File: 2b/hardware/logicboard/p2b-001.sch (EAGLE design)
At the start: 76 parts, among them IC1 74LS06N, IC2 4066N, J1 MKR, J10 1-Wire, J2 GPIO, J20 GPIO, J3 Vcc, J4** RLY2, J5 SPI, J6 LED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

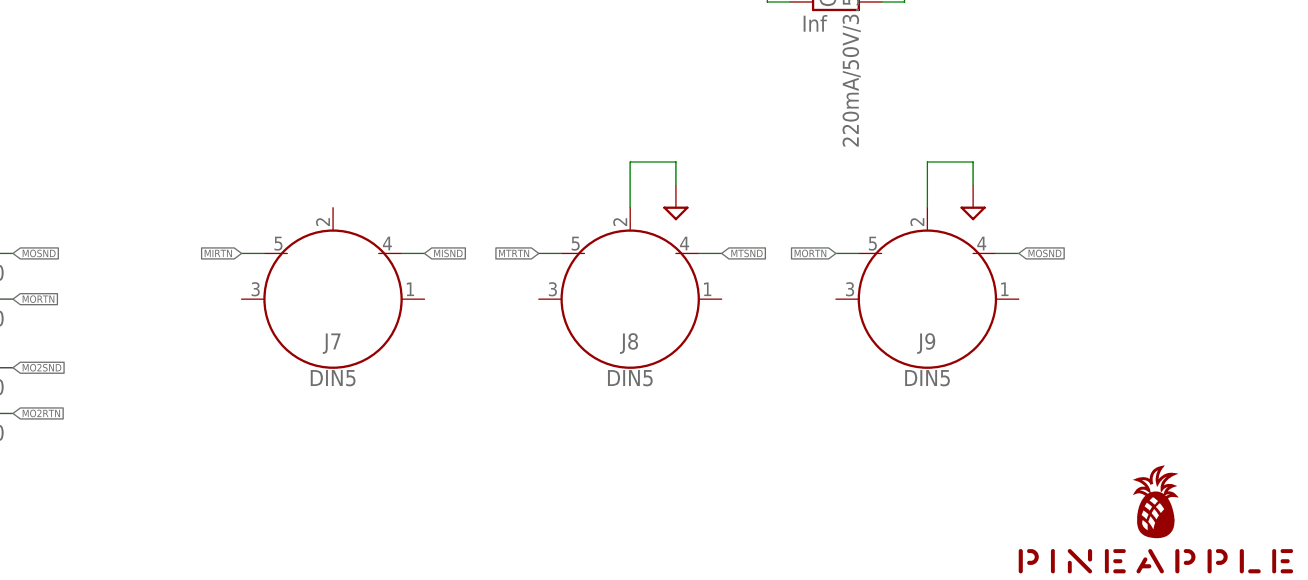
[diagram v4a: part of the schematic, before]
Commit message: Now P2b has phantom power.
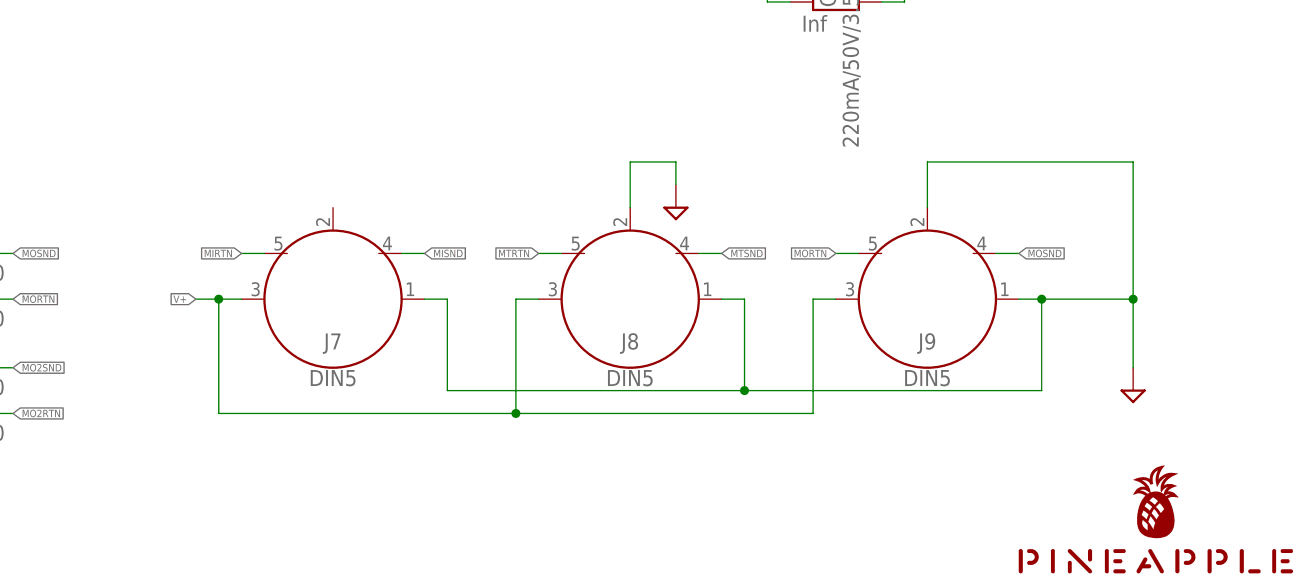
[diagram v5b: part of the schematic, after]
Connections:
- net GND: now also J7.1, J8.1, J9.1
- net V+: now also J7.3, J8.3, J9.3
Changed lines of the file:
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@@
 </instance>
 <instance part="SUPPLY16" gate="GND" x="259.08" y="48.26" smashed="yes"/>
-<instance part="SUPPLY17" gate="GND" x="292.1" y="48.26" smashed="yes"/>
+<instance part="SUPPLY17" gate="GND" x="309.88" y="27.94" smashed="yes"/>
 <instance part="SUPPLY19" gate="G$1" x="167.64" y="170.18" smashed="yes">
 <attribute name="VALUE" x="167.64" y="175.26" size="1.778" layer="96" align="bottom-center"/>
@@
 <pinref part="J9" gate="G$1" pin="2"/>
 <wire x1="287.02" y1="48.26" x2="287.02" y2="53.34" width="0.1524" layer="91"/>
-<wire x1="287.02" y1="53.34" x2="292.1" y2="53.34" width="0.1524" layer="91"/>
+<wire x1="287.02" y1="53.34" x2="309.88" y2="53.34" width="0.1524" layer="91"/>
 <pinref part="SUPPLY17" gate="GND" pin="GND"/>
-<wire x1="292.1" y1="53.34" x2="292.1" y2="50.8" width="0.1524" layer="91"/>
+<wire x1="309.88" y1="53.34" x2="309.88" y2="38.1" width="0.1524" layer="91"/>
+<pinref part="J9" gate="G$1" pin="1"/>
+<wire x1="309.88" y1="38.1" x2="309.88" y2="30.48" width="0.1524" layer="91"/>
+<wire x1="297.18" y1="38.1" x2="299.72" y2="38.1" width="0.1524" layer="91"/>
+<junction x="309.88" y="38.1"/>
+<pinref part="J8" gate="G$1" pin="1"/>
+<wire x1="299.72" y1="38.1" x2="309.88" y2="38.1" width="0.1524" layer="91"/>
+<wire x1="264.16" y1="38.1" x2="266.7" y2="38.1" width="0.1524" layer="91"/>
+<wire x1="266.7" y1="38.1" x2="266.7" y2="27.94" width="0.1524" layer="91"/>
+<wire x1="266.7" y1="27.94" x2="299.72" y2="27.94" width="0.1524" layer="91"/>
+<wire x1="299.72" y1="27.94" x2="299.72" y2="38.1" width="0.1524" layer="91"/>
+<junction x="299.72" y="38.1"/>
+<pinref part="J7" gate="G$1" pin="1"/>
+<wire x1="231.14" y1="38.1" x2="233.68" y2="38.1" width="0.1524" layer="91"/>
+<wire x1="233.68" y1="38.1" x2="233.68" y2="27.94" width="0.1524" layer="91"/>
+<wire x1="233.68" y1="27.94" x2="266.7" y2="27.94" width="0.1524" layer="91"/>
+<junction x="266.7" y="27.94"/>
 </segment>
 <segment>
@@
 <label x="66.04" y="200.66" size="1.778" layer="95"/>
 </segment>
-</net>
+<segment>
+<pinref part="J9" gate="G$1" pin="3"/>
+<wire x1="276.86" y1="38.1" x2="274.32" y2="38.1" width="0.1524" layer="91"/>
+<wire x1="274.32" y1="38.1" x2="274.32" y2="25.4" width="0.1524" layer="91"/>
+<pinref part="J7" gate="G$1" pin="3"/>
+<wire x1="210.82" y1="38.1" x2="208.28" y2="38.1" width="0.1524" layer="91"/>
+<label x="205.74" y="38.1" size="0.8128" layer="95" rot="R180" xref="yes"/>
+<wire x1="208.28" y1="38.1" x2="205.74" y2="38.1" width="0.1524" layer="91"/>
+<wire x1="208.28" y1="38.1" x2="208.28" y2="25.4" width="0.1524" layer="91"/>
+<wire x1="208.28" y1="25.4" x2="241.3" y2="25.4" width="0.1524" layer="91"/>
+<junction x="208.28" y="38.1"/>
+<pinref part="J8" gate="G$1" pin="3"/>
+<wire x1="243.84" y1="38.1" x2="241.3" y2="38.1" width="0.1524" layer="91"/>
+<wire x1="241.3" y1="25.4" x2="241.3" y2="38.1" width="0.1524" layer="91"/>
+<wire x1="274.32" y1="25.4" x2="241.3" y2="25.4" width="0.1524" layer="91"/>
+<junction x="241.3" y="25.4"/>
+</segment>
+</net>

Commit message: Added SW.
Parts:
- added S2: (no value), switch-dil:DIP02YL
- V1: device v-reg:78XXL -> v-reg:78XXS
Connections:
- new net MIDIINV+: J7.3, S2.1
- new net MIDIOUTV+: J8.3, J9.3, S2.2
- net V+: now also S2.3, S2.4; no longer J7.3, J8.3, J9.3
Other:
- moved on the sheet: J7, J8, J9

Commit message: Now has a phantom SW.
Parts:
- S2: device switch-dil:DIP02YL -> switch-dil:DIP04YL
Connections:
- new net MIDIINGND: J7.1, S2.1
- new net MIDIOUTGND: J8.1, J9.1, S2.3
- net GND: now also S2.6, S2.8; no longer J7.1, J8.1, J9.1
- net MIDIINV+: now also S2.2; no longer S2.1
- net MIDIOUTV+: now also S2.4; no longer S2.2
- net V+: now also S2.5, S2.7; no longer S2.3, S2.4
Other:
- moved on the sheet: J7, J8, J9

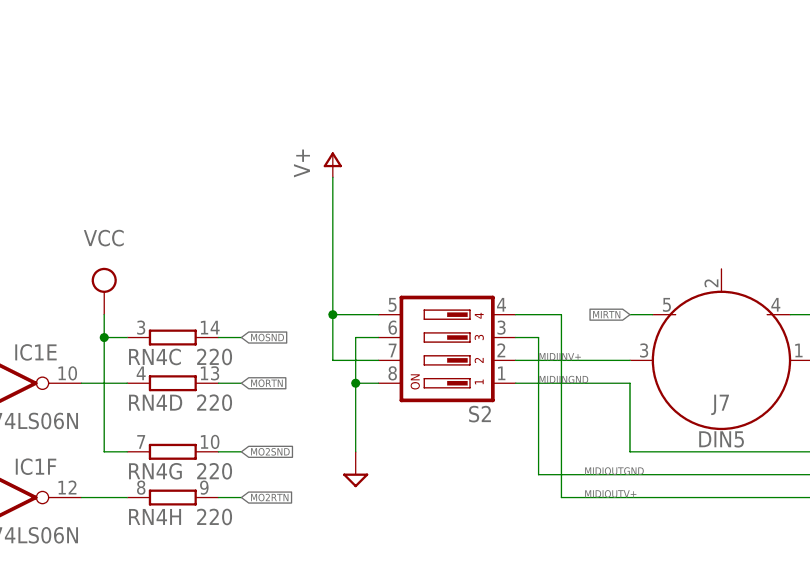
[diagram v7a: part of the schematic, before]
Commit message: GND pattern.
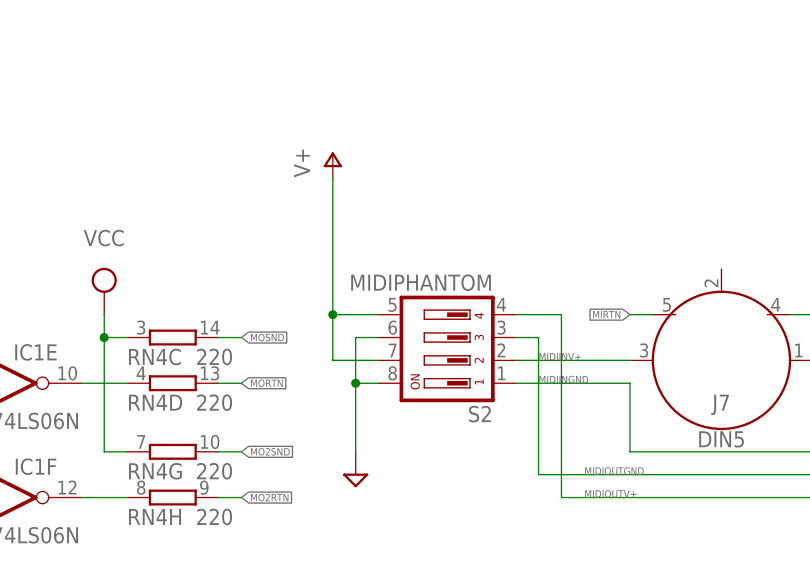
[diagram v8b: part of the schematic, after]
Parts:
- S2: value (none) -> MIDIPHANTOM
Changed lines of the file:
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@@
 <part name="RZ04" library="rcl" library_urn="urn:adsk.eagle:library:334" deviceset="R-EU_" device="M2012" package3d_urn="urn:adsk.eagle:package:23561/2" value="Inf"/>
 <part name="P+5" library="supply1" library_urn="urn:adsk.eagle:library:371" deviceset="V+" device=""/>
-<part name="S2" library="switch-dil" library_urn="urn:adsk.eagle:library:375" deviceset="DIP04YL" device="" package3d_urn="urn:adsk.eagle:package:27255/2"/>
+<part name="S2" library="switch-dil" library_urn="urn:adsk.eagle:library:375" deviceset="DIP04YL" device="" package3d_urn="urn:adsk.eagle:package:27255/2" value="MIDIPHANTOM"/>
 <part name="SUPPLY16" library="supply2" deviceset="GND" device=""/>
 </parts>
